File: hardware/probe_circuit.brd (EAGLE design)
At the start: 100 x 80 mm, 2 parts, among them U1 LT1920CS8PBF

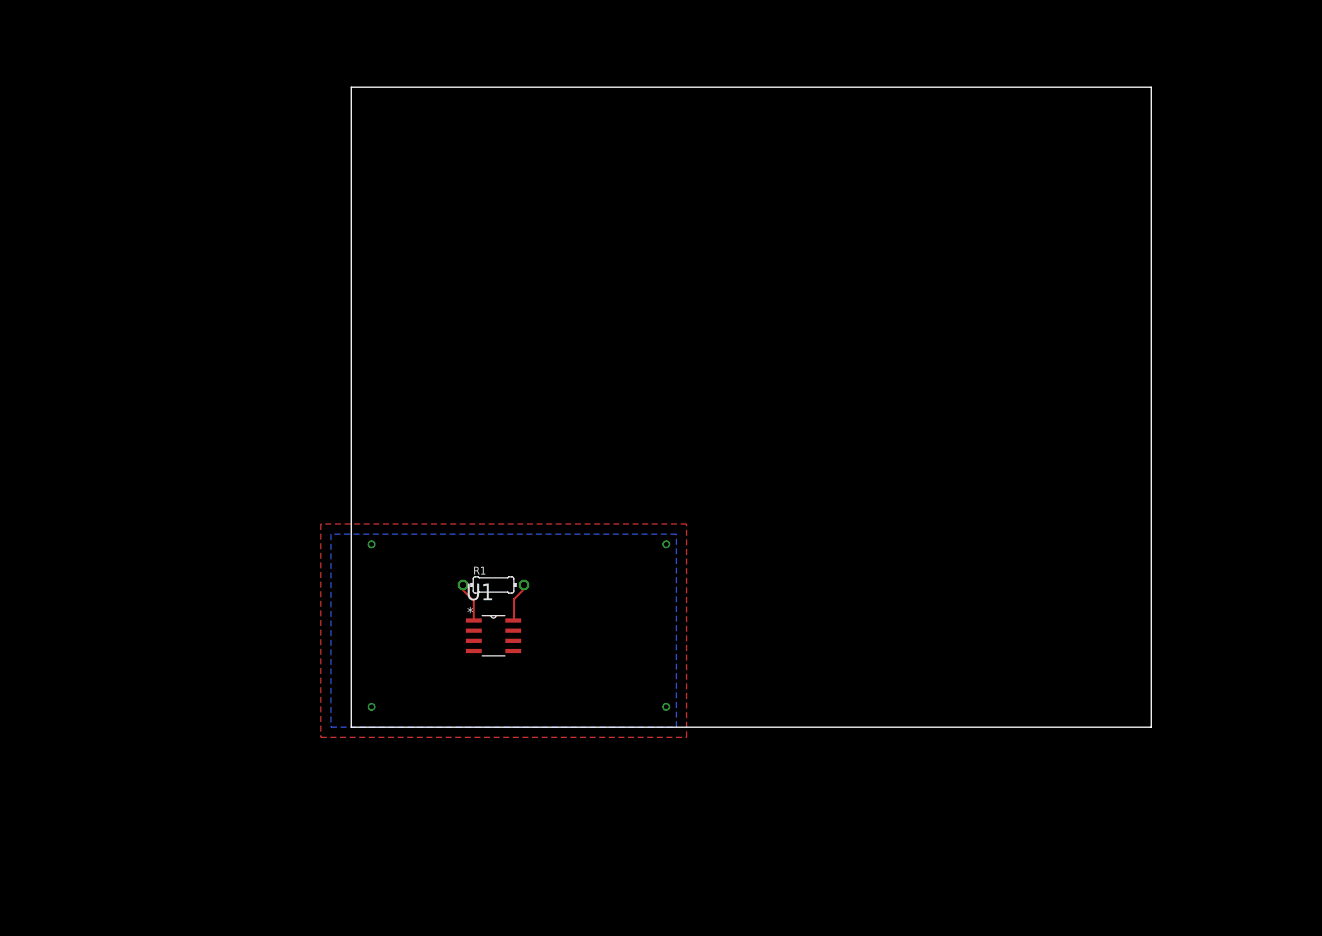
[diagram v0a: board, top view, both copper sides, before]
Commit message: - updated PCB
- added example switches, connector points and resistors to the board
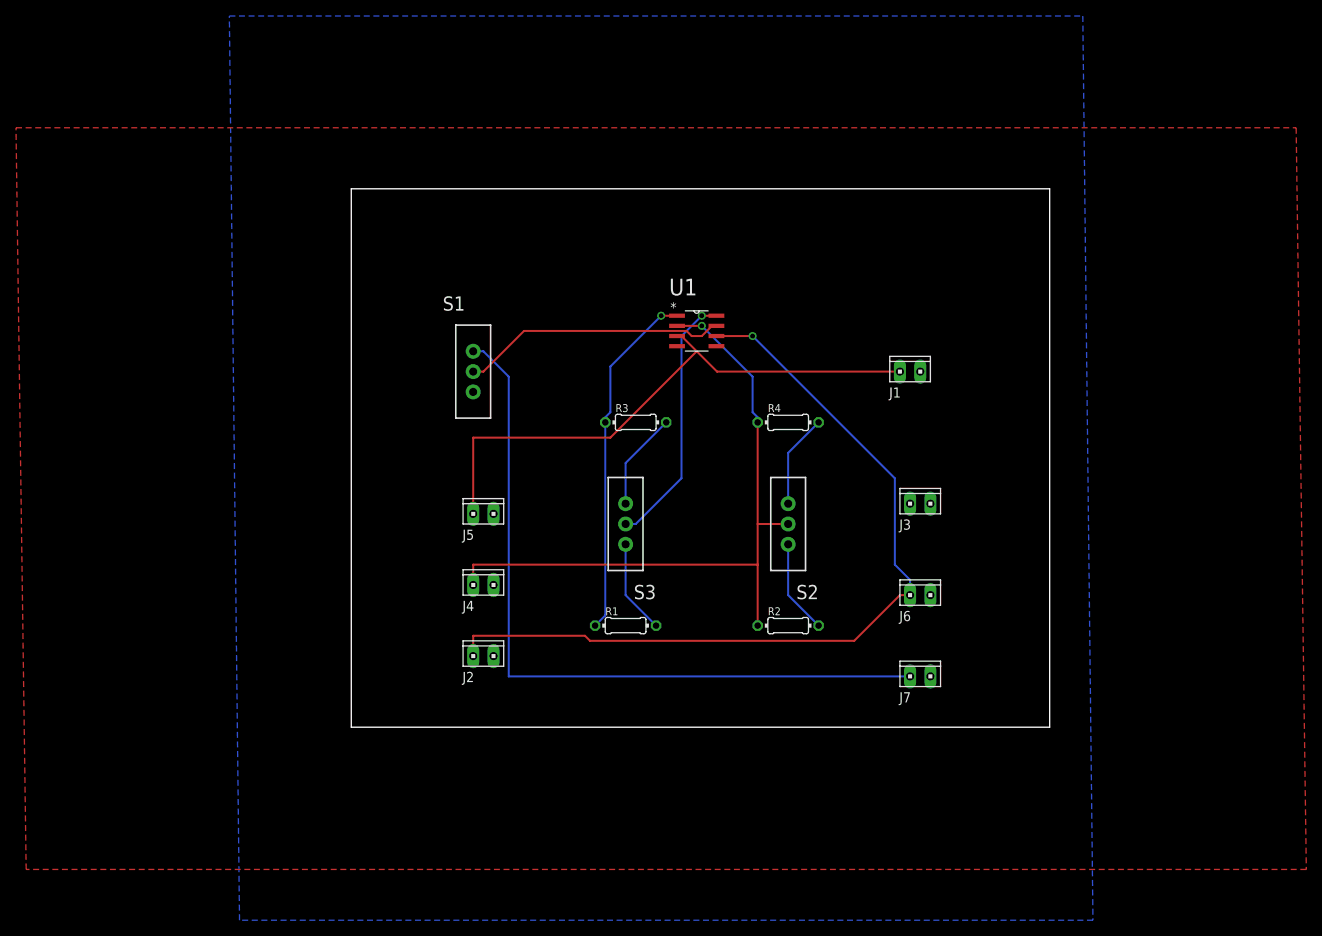
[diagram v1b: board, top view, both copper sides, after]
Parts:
- added J1, J5: VPD, con-amp:10X02MTA
- added J2, J6: VSIG, con-amp:10X02MTA
- added J3: VLED, con-amp:10X02MTA
- added J4: VOFF, con-amp:10X02MTA
- added J7: VCC_IN, con-amp:10X02MTA
- added R2: 10k, eagle-ltspice:0204/7
- added R3: 0-5k, eagle-ltspice:0204/7
- added R4: 0-10k, eagle-ltspice:0204/7
- added S1: ON/OFF, SparkFun-Electromechanical:SWITCH-SPDT
- added S2: OFFSET, SparkFun-Electromechanical:SWITCH-SPDT
- added S3: GAIN, SparkFun-Electromechanical:SWITCH-SPDT
- moved U1 45.8 mm to (43.2, 49.5)
- moved R1 17.3 mm to (34.3, 12.7)
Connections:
- new net RG_1: R3.2, S3.3
- new net RG_X: S3.2, U1.8
- new net VCC_IN: J7.2, S1.1
- new net VLED: J3.2
- new net VOFF_1: R4.2, S2.3
- new net VOFF_2: R2.2, S2.1
- net GND: now also J1.1, J2.1, J3.1, J4.1, J5.1, J6.1, J7.1, S1.3
- net RG: now also R3.1
- net RG_2: now also S3.1; no longer U1.8
- net VCC: now also S1.2
- net VOFF: now also J4.2, R2.1, R4.1, S2.2
- net VPD: now also J1.2, J5.2
- net VSIG: now also J2.2, J6.2
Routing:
- net VSIG: track 0.00 -> 104.8 mm, vias 0 -> 1
- net VCC_IN: track 0.00 -> 93.4 mm
- net VOFF: track 0.00 -> 85.4 mm, vias 0 -> 1
- net VPD: track 0.00 -> 71.6 mm
- net RG: track 5.01 -> 44.1 mm, vias 0 -> 1
- net VCC: track 0.00 -> 33.3 mm
- net RG_X: track 0.00 -> 32.6 mm, vias 0 -> 1
- net RG_1: track 0.00 -> 12.3 mm
- net VOFF_2: track 0.00 -> 11.7 mm
- net VOFF_1: track 0.00 -> 11.7 mm
- net RG_2: track 4.98 -> 11.7 mm
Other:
- board size 100 x 80 mm -> 87.3 x 67.3 mm

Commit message: Added connectors for variable resisotrs and conmpressed board.
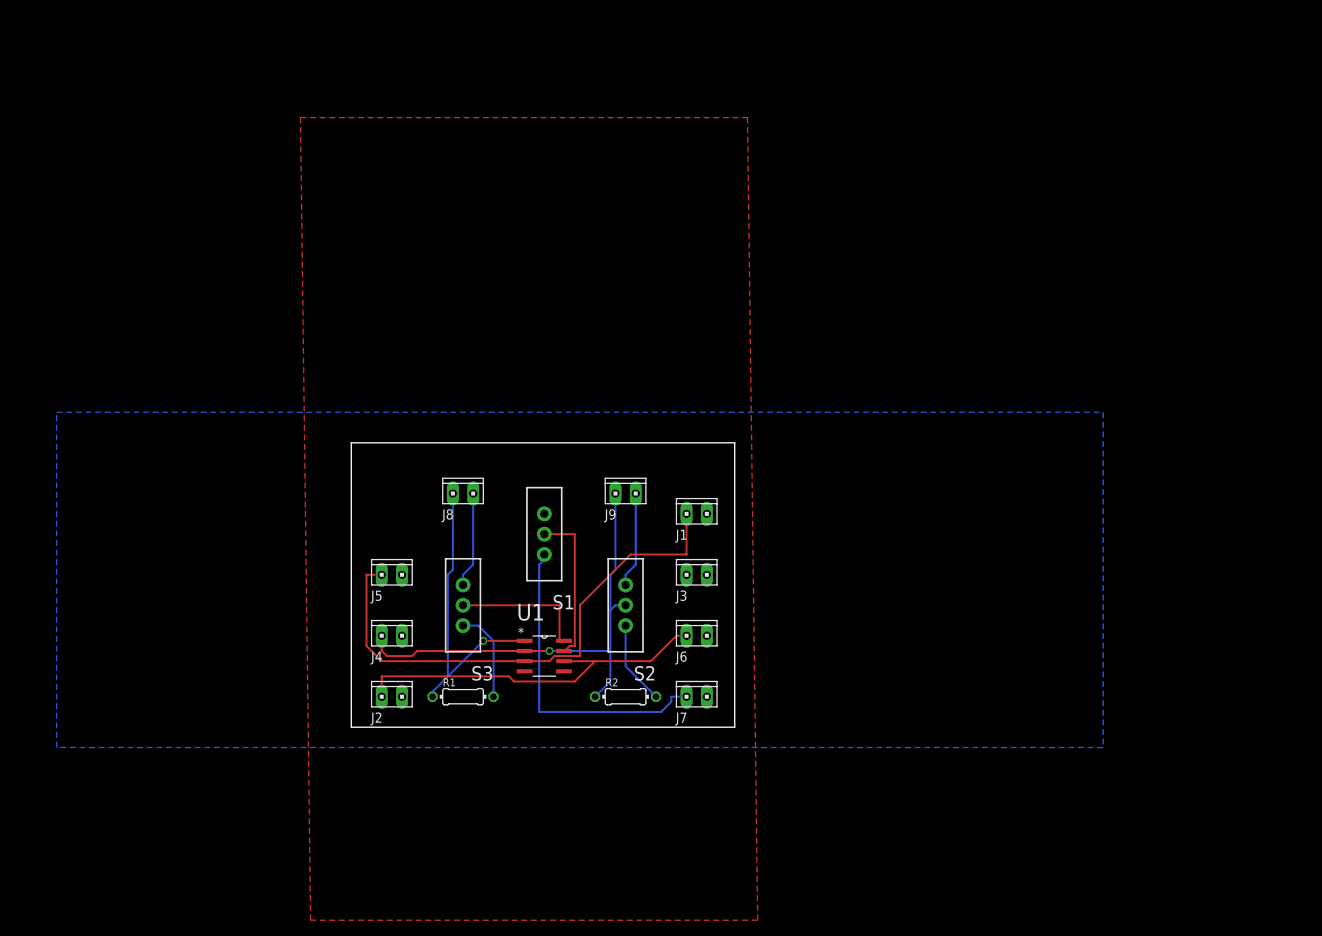
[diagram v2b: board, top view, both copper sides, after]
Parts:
- removed R3: 0-5k, eagle-ltspice:0204/7
- removed R4: 0-10k, eagle-ltspice:0204/7
- added J8: 0-5k, con-amp:10X02MTA
- added J9: 0-10k, con-amp:10X02MTA
- moved U1 44.9 mm to (24.1, 8.89)
- moved J1 32.1 mm to (43.2, 26.7)
- moved J3 29.3 mm to (43.2, 19.1)
- moved J6 28.4 mm to (43.2, 11.4)
- moved J7 28.1 mm to (43.2, 3.81)
- moved S2 22.7 mm to (34.3, 15.2)
- moved S3 22.7 mm to (14.0, 15.2)
- moved S1 22.2 mm to (24.1, 24.1), turned to 180 degrees
- moved R1 22.2 mm to (14.0, 3.81)
- moved R2 22.2 mm to (34.3, 3.81)
- moved J5 13.7 mm to (5.08, 19.1)
- moved J4 13.1 mm to (5.08, 11.4)
- moved J2 12.5 mm to (5.08, 3.81)
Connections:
- net RG: now also J8.2; no longer R3.1
- net RG_1: now also J8.1; no longer R3.2
- net VOFF: now also J9.2; no longer R4.1
- net VOFF_1: now also J9.1; no longer R4.2
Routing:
- net VSIG: track 104.8 -> 47.2 mm, vias 1 -> 0
- net VCC_IN: track 93.4 -> 39.5 mm
- net VOFF: track 85.4 -> 59.6 mm
- net RG_X: track 32.6 -> 17.1 mm, vias 1 -> 0
- net VCC: track 33.3 -> 19.4 mm
- net RG: track 44.1 -> 37.9 mm
- net VPD: track 71.6 -> 65.9 mm
- net VOFF_2: track 11.7 -> 10.5 mm
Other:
- board size 87.3 x 67.3 mm -> 47.9 x 35.5 mm
